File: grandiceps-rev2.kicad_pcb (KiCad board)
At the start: 2 copper layers, 149.8 x 115.9 mm, 107 parts, among them J1 MJ-4PP-9, SW1 ESC, SW10 E, SW11 R, SW12 T, SW13 CAPS, SW14 A, SW15 S, SW16 D, SW17 F, SW18 G, SW19 SHIFT, SW2 1, SW20 <, SW21 Z, SW22 X, SW23 C, SW24 V, SW25 CTRL, SW26 SUPER, SW27 ALT, SW28 X, SW29 C, SW3 2, SW30 Rotary_Encoder_Switch, SW4 3, SW5 4, SW6 5, SW7 TAB, SW8 Q, SW9 W, U1 WeActBlackPill, U2 24LC64

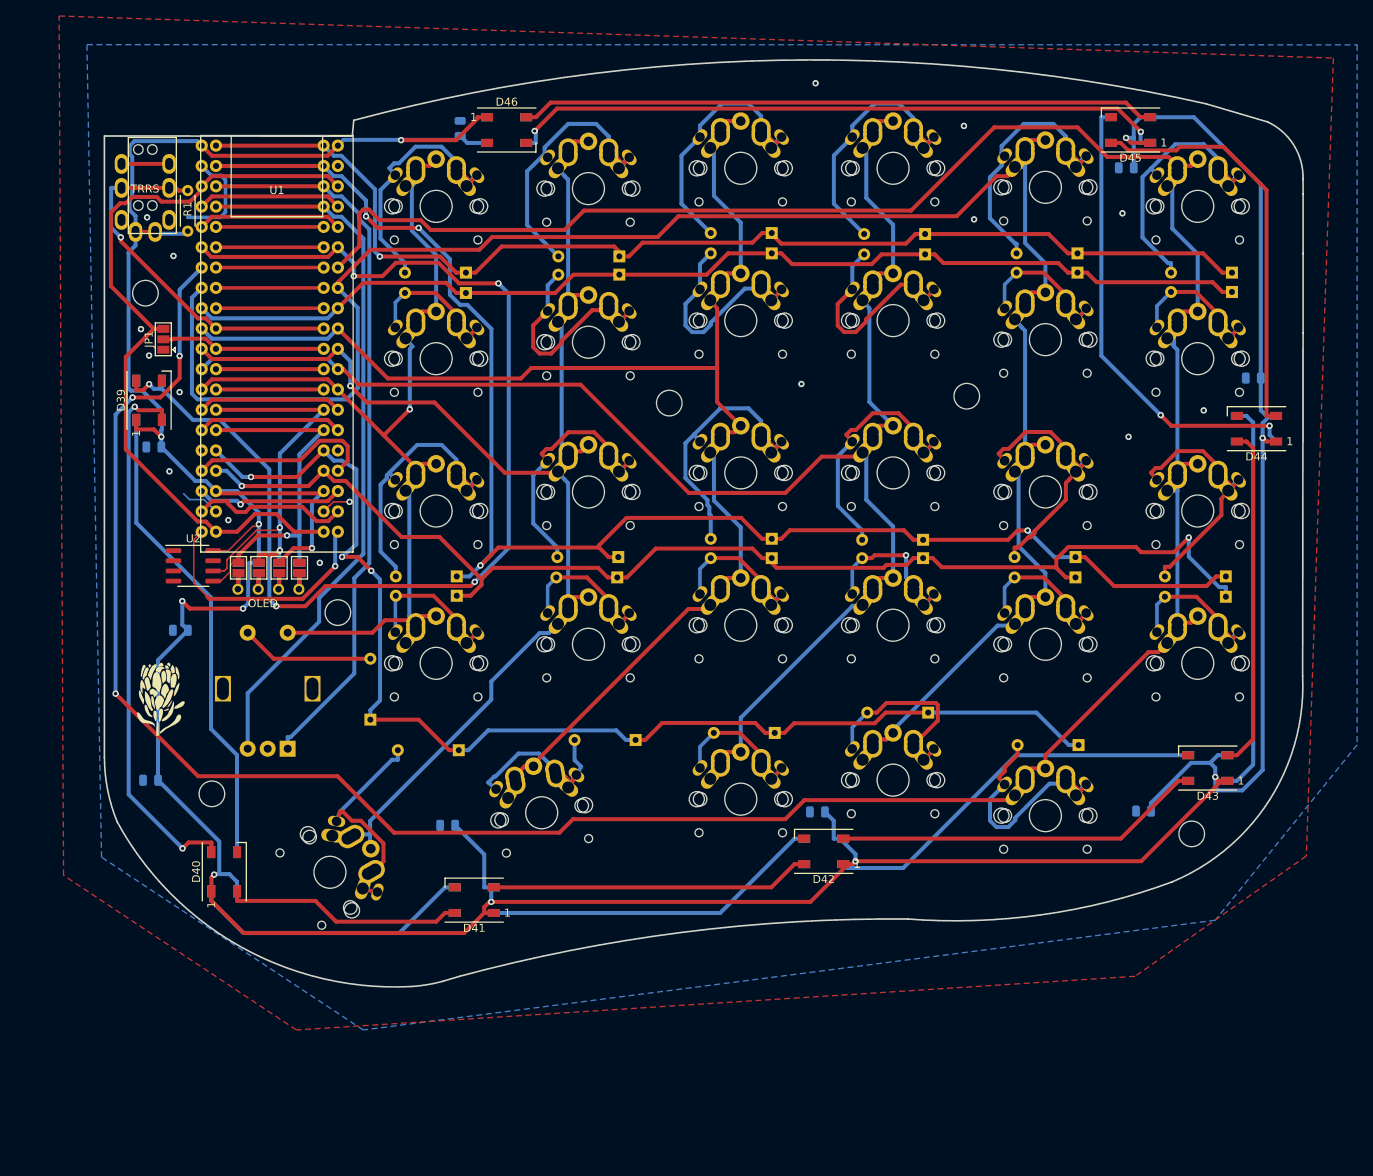
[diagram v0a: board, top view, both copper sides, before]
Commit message: Add trackpoint , move thumb
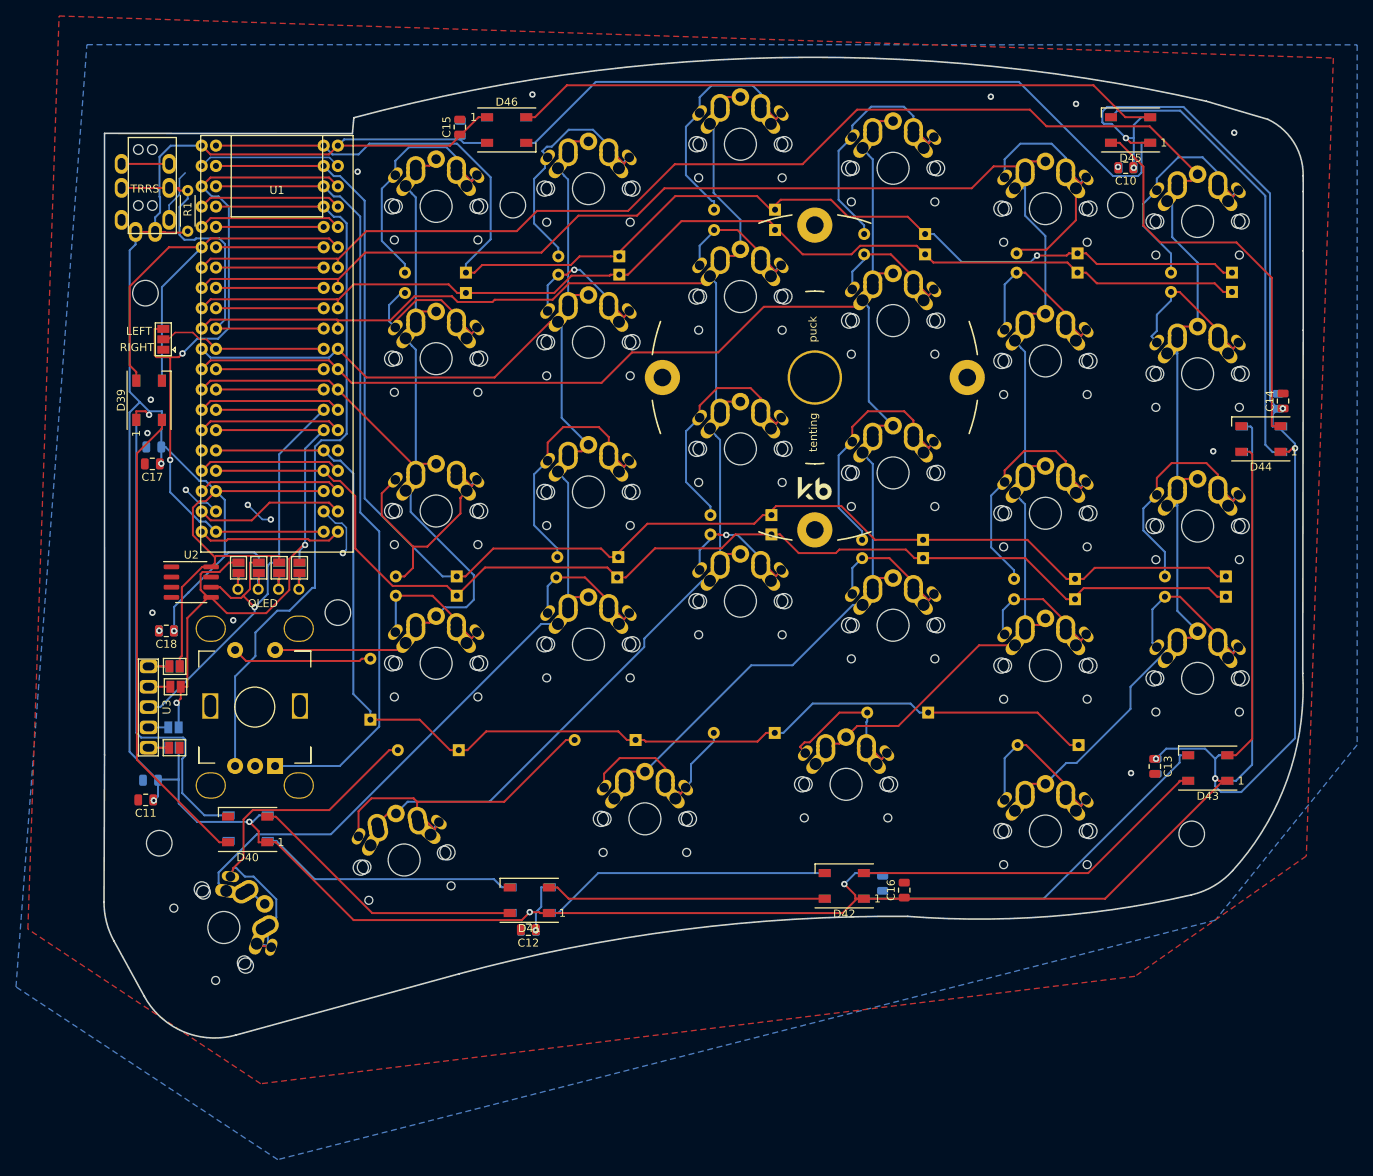
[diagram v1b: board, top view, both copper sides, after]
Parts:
- removed G*** (x2): LOGO, gcp:Protea-tiny
- added C10: 100nF, Capacitor_SMD:C_0805_2012Metric, F.Cu at (216.3, 49.9)
- added C11: 100nF, Capacitor_SMD:C_0805_2012Metric, F.Cu at (93.8, 128.9)
- added C12: 100nF, Capacitor_SMD:C_0805_2012Metric, F.Cu at (141.6, 145.2)
- added C13: 100nF, Capacitor_SMD:C_0805_2012Metric, F.Cu at (219.9, 124.8)
- added C14: 100nF, Capacitor_SMD:C_0805_2012Metric, F.Cu at (236.0, 79.1)
- added C15: 100nF, Capacitor_SMD:C_0805_2012Metric, F.Cu at (133.1, 44.8)
- added C16: 100nF, Capacitor_SMD:C_0805_2012Metric, F.Cu at (188.6, 140.2)
- added C17: 100nF, Capacitor_SMD:C_0805_2012Metric, F.Cu at (94.6, 87.0)
- added C18: 100nF, Capacitor_SMD:C_0805_2012Metric, F.Cu at (96.4, 107.8)
- added JP10: Jumper_NO_Small, Jumper:SolderJumper-2_P1.3mm_Open_Pad1.0x1.5mm, B.Cu at (97.4, 112.3)
- added JP11: Jumper_NO_Small, Jumper:SolderJumper-2_P1.3mm_Open_Pad1.0x1.5mm, F.Cu at (97.4, 122.4)
- added JP12: Jumper_NO_Small, Jumper:SolderJumper-2_P1.3mm_Open_Pad1.0x1.5mm, B.Cu at (97.3, 122.4)
- added JP13: Jumper_NO_Small, Jumper:SolderJumper-2_P1.3mm_Open_Pad1.0x1.5mm, F.Cu at (97.4, 112.3)
- added JP14: Jumper_NO_Small, Jumper:SolderJumper-2_P1.3mm_Open_Pad1.0x1.5mm, B.Cu at (97.3, 119.9)
- added JP15: Jumper_NO_Small, Jumper:SolderJumper-2_P1.3mm_Open_Pad1.0x1.5mm, F.Cu at (97.5, 114.8)
- added REF**: Tenting Puck, gcp:Tenting_Puck, F.Cu at (177.4, 76.2)
- added U3: PIM447, gcp:pimoroni-trackballl-bommod, F.Cu at (107.4, 117.3)
- moved H6 31.5 mm to (139.7, 54.6)
- moved H2 30.6 mm to (215.6, 54.6)
- moved SW28 18.2 mm to (126.1, 136.5)
- moved C1 16.6 mm to (141.7, 145.2)
- moved SW29 15.0 mm to (103.6, 144.9)
- moved SW27 12.2 mm to (156.2, 131.3)
- moved C4 12.1 mm to (185.9, 139.4), turned to -90 degrees
- moved H9 9.02 mm to (95.5, 134.4)
- moved D33 7.00 mm to (141.9, 141.5)
- moved D41 6.88 mm to (141.8, 141.5)
- moved D32 6.22 mm to (106.6, 132.5), turned to 180 degrees
- moved D40 6.03 mm to (106.5, 132.7), turned to 180 degrees
- moved SW26 5.90 mm to (181.4, 127.0)
- moved C8 5.82 mm to (220.1, 124.8), turned to -90 degrees
- moved D34 5.03 mm to (181.2, 139.7)
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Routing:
- net col0: track 396.3 -> 244.4 mm, vias 3 -> 0
- net RGB: track 149.0 -> 59.8 mm, vias 5 -> 0
- net +5V: track 517.7 -> 568.5 mm, vias 12 -> 14
- net col3: track 171.3 -> 203.2 mm
- net SDA: track 45.5 -> 77.2 mm, vias 1 -> 2
- net col4: track 163.6 -> 188.7 mm, vias 1 -> 0
- net SCL: track 49.9 -> 73.5 mm, vias 2 -> 1
- net Net-(D29-Pad2): track 27.3 -> 49.2 mm
- net Net-(D28-Pad2): track 21.5 -> 42.7 mm
- net col1: track 236.8 -> 217.4 mm
- net GND: track 21.6 -> 40.2 mm, vias 16 -> 17
- net col2: track 190.1 -> 205.3 mm
- net col5: track 114.6 -> 129.2 mm, vias 1 -> 0
- net unconnected-(U1-Pad20): track 31.2 -> 18.1 mm, vias 1 -> 0
- net row0: track 144.9 -> 157.0 mm
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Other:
- board size 149.8 x 115.9 mm -> 149.9 x 122.6 mm
- board text added: "LEFT"
- board text added: "RIGHT"
